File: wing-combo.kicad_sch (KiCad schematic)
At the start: 0 parts

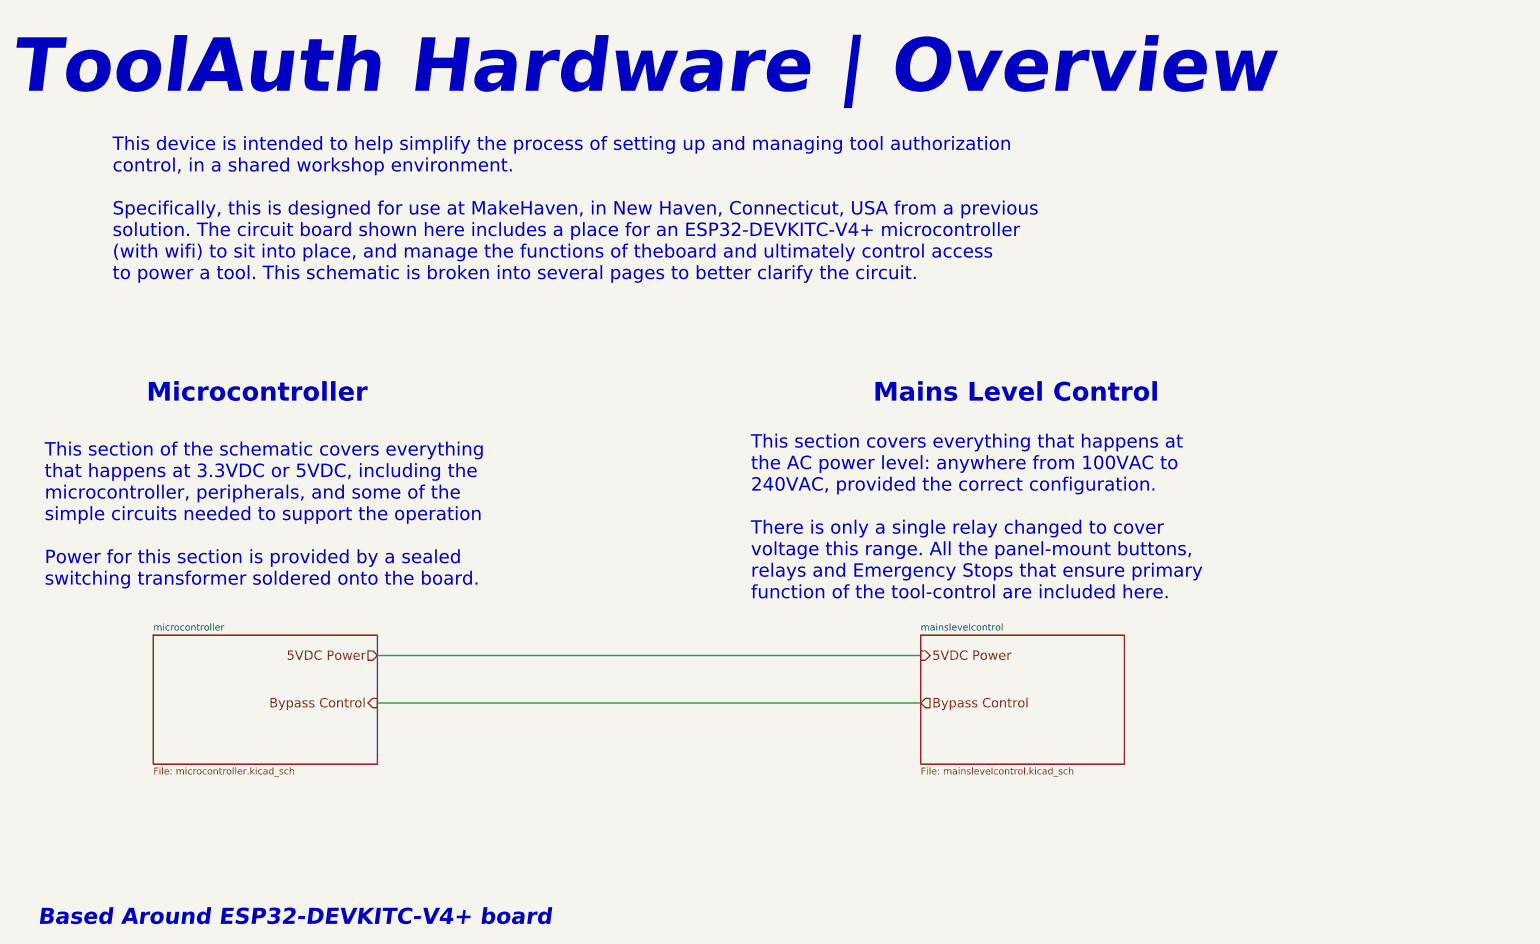
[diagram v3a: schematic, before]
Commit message: moved LED GPIO to fit free pins for ethernet wing
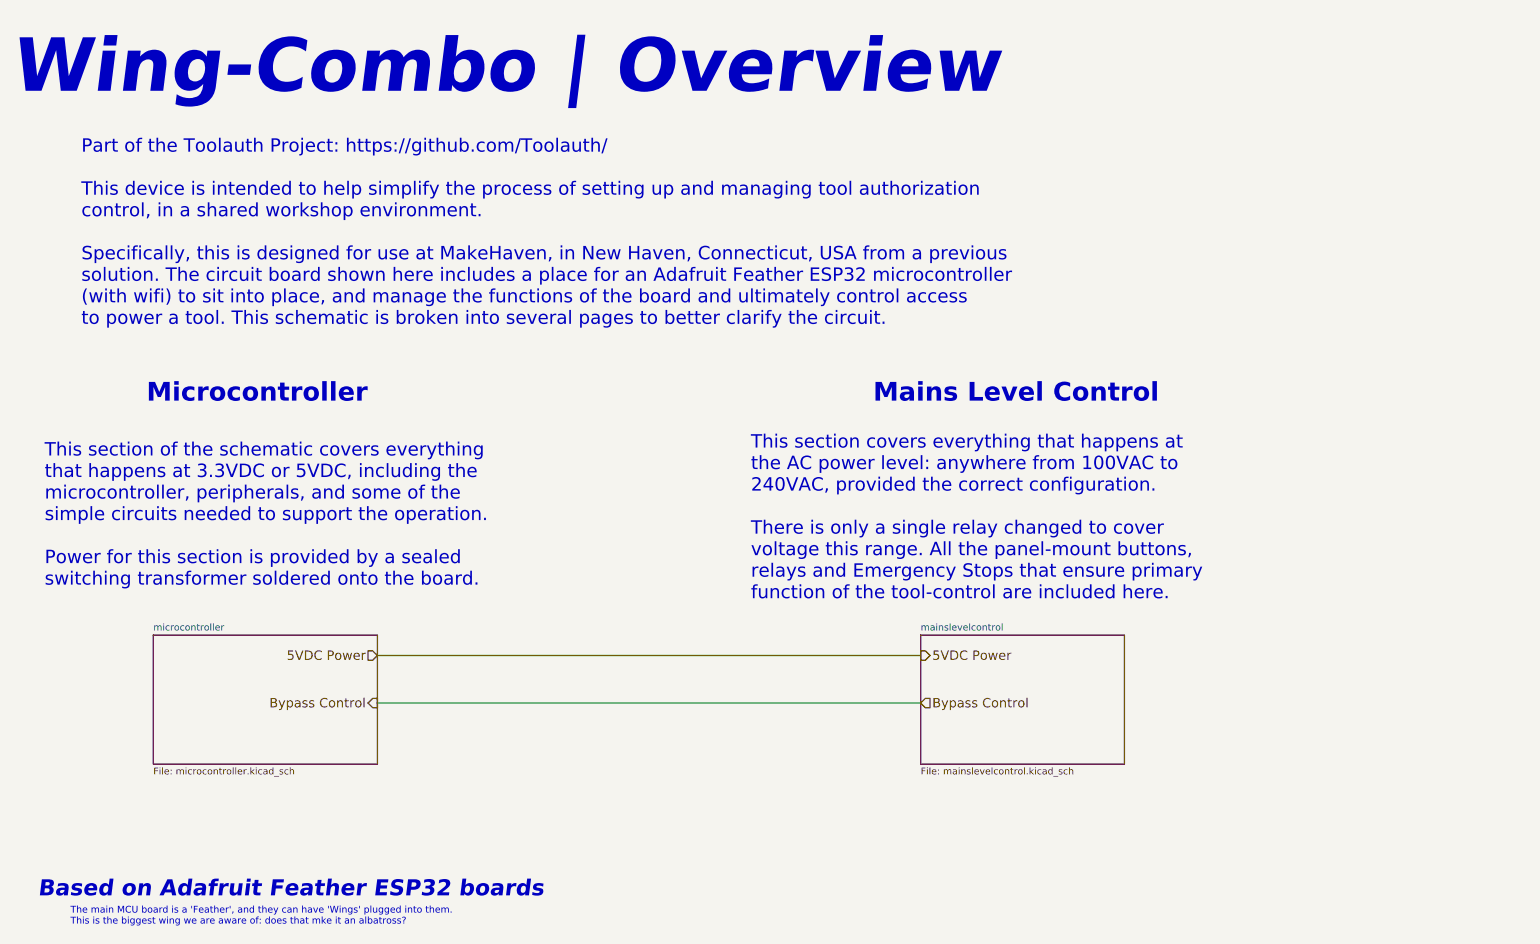
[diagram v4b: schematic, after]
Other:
- note added: "Based on Adafruit Feather ESP32 boards"
- note added: "Part of the Toolauth Project: https://github.com/Toolauth/ This device is intended to help simplify the process of setting up and managing tool authorization control, in a shared workshop environment. Specifically, this is designed for use at MakeHaven, in New Haven, Connecticut, USA from a previous solution. The circuit board shown here includes a place for an Adafruit Feather ESP32 microcontrol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"
- note added: "The main MCU board is a 'Feather', and they can have 'Wings' plugged into them. This is the biggest wing we are aware of: does that mke it an albatross?"
- note added: "This section of the schematic covers everything that happens at 3.3VDC or 5VDC, including the microcontroller, peripherals, and some of the simple circuits needed to support the operation. Power for this section is provided by a sealed switching transformer soldered onto the board."
- note added: "Wing-Combo | Overview"
- note removed: "Based Around ESP32-DEVKITC-V4+ board"
- note removed: "This device is intended to help simplify the process of setting up and managing tool authorization control, in a shared workshop environment. Specifically, this is designed for use at MakeHaven, in New Haven, Connecticut, USA from a previous solution. The circuit board shown here includes a place for an ESP32-DEVKITC-V4+ microcontroller (with wifi) to sit into place, and manage the functions of t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"
- note removed: "This section of the schematic covers everything that happens at 3.3VDC or 5VDC, including the microcontroller, peripherals, and some of the simple circuits needed to support the operation Power for this section is provided by a sealed switching transformer soldered onto the board."
- note removed: "ToolAuth Hardware | Overview"
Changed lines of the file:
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@@
 		)
 	)
-	(text "ToolAuth Hardware | Overview"
+	(text "The main MCU board is a 'Feather', and they can have 'Wings' plugged into them. \nThis is the biggest wing we are aware of: does that mke it an albatross?"
+		(exclude_from_sim no)
+		(at 34.036 189.738 0)
+		(effects
+			(font
+				(size 1.27 1.27)
+			)
+			(justify left)
+		)
+	)
+	(text "Wing-Combo | Overview"
 		(exclude_from_sim no)
 		(at 22.86 36.83 0)
@@
 		)
 	)
-	(text "This section of the schematic covers everything \nthat happens at 3.3VDC or 5VDC, including the \nmicrocontroller, peripherals, and some of the \nsimple circuits needed to support the operation \n\nPower for this section is provided by a sealed \nswitching transformer soldered onto the board. "
+	(text "This section of the schematic covers everything \nthat happens at 3.3VDC or 5VDC, including the \nmicrocontroller, peripherals, and some of the \nsimple circuits needed to support the operation.\n\nPower for this section is provided by a sealed \nswitching transformer soldered onto the board. "
 		(exclude_from_sim no)
 		(at 29.21 128.27 0)
@@
 		)
 	)
-	(text "This device is intended to help simplify the process of setting up and managing tool authorization \ncontrol, in a shared workshop environment. \n\nSpecifically, this is designed for use at MakeHaven, in New Haven, Connecticut, USA from a previous\nsolution. The circuit board shown here includes a place for an ESP32-DEVKITC-V4+ microcontroller \n(with wifi) to sit into place, and manage the functions of theboard and ultimately control access \nto power a tool. This schematic is broken into several pages to better clarify the circuit.\n"
+	(text "Part of the Toolauth Project: https://github.com/Toolauth/\n\nThis device is intended to help simplify the process of setting up and managing tool authorization \ncontrol, in a shared workshop environment. \n\nSpecifically, this is designed for use at MakeHaven, in New Haven, Connecticut, USA from a previous\nsolution. The circuit board shown here includes a place for an Adafruit Feather ESP32 microcontroller \n(with wifi) to sit into place, and manage the functions of the board and ultimately control access \nto power a tool. This schematic is broken into several pages to better clarify the circuit.\n"
 		(exclude_from_sim no)
-		(at 41.91 71.12 0)
+		(at 36.068 79.502 0)
 		(effects
 			(font
@@
 			)
 			(justify left bottom)
+			(href "https://github.com/Toolauth/")
 		)
 	)
@@
 		)
 	)
-	(text "Based Around ESP32-DEVKITC-V4+ board"
+	(text "Based on Adafruit Feather ESP32 boards"
 		(exclude_from_sim no)
-		(at 27.94 191.77 0)
+		(at 27.94 186.436 0)
 		(effects
 			(font

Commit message: 1.4.1 schematic update
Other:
- note added: "Toolauth | Wing-Combo"
- note added: "feather specification: https://learn.adafruit.com/adafruit-feather/feather-specification"
- note removed: "Wing-Combo | Overview"
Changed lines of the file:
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@@
 	(text "The main MCU board is a 'Feather', and they can have 'Wings' plugged into them. \nThis is the biggest wing we are aware of: does that mke it an albatross?"
 		(exclude_from_sim no)
-		(at 34.036 189.738 0)
+		(at 39.624 184.404 0)
 		(effects
 			(font
@@
 		)
 	)
-	(text "Wing-Combo | Overview"
+	(text "Toolauth | Wing-Combo"
 		(exclude_from_sim no)
 		(at 22.86 36.83 0)
@@
 			)
 			(justify left bottom)
+		)
+	)
+	(text "feather specification: https://learn.adafruit.com/adafruit-feather/feather-specification"
+		(exclude_from_sim no)
+		(at 80.264 190.5 0)
+		(effects
+			(font
+				(size 1.27 1.27)
+			)
+			(href "https://learn.adafruit.com/adafruit-feather/feather-specification")
 		)
 	)
@@
 	(text "Based on Adafruit Feather ESP32 boards"
 		(exclude_from_sim no)
-		(at 27.94 186.436 0)
+		(at 33.528 181.102 0)
 		(effects
 			(font

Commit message: close enough for 3D export
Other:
- note added: "The main MCU board is a 'Feather', and they can have 'Wings' plugged into them. This is the biggest wing we are aware of: does that make it an albatross?"
- note added: "This section covers everything that happens at the AC power level: anywhere from 100VAC to 240VAC, provided the corresponding configuration. There is only a single relay changed to cover voltage this range. All the panel-mount buttons, relays and Emergency Stops that ensure primary function of the tool-control are included here."
- note removed: "The main MCU board is a 'Feather', and they can have 'Wings' plugged into them. This is the biggest wing we are aware of: does that mke it an albatross?"
- note removed: "This section covers everything that happens at the AC power level: anywhere from 100VAC to 240VAC, provided the correct configuration. There is only a single relay changed to cover voltage this range. All the panel-mount buttons, relays and Emergency Stops that ensure primary function of the tool-control are included here."
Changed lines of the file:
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@@
 		)
 	)
-	(text "The main MCU board is a 'Feather', and they can have 'Wings' plugged into them. \nThis is the biggest wing we are aware of: does that mke it an albatross?"
+	(text "The main MCU board is a 'Feather', and they can have 'Wings' plugged into them. \nThis is the biggest wing we are aware of: does that make it an albatross?"
 		(exclude_from_sim no)
-		(at 39.624 184.404 0)
+		(at 41.148 181.102 0)
 		(effects
 			(font
@@
 	(text "feather specification: https://learn.adafruit.com/adafruit-feather/feather-specification"
 		(exclude_from_sim no)
-		(at 80.264 190.5 0)
+		(at 81.788 187.198 0)
 		(effects
 			(font
@@
 		)
 	)
-	(text "This section covers everything that happens at \nthe AC power level: anywhere from 100VAC to \n240VAC, provided the correct configuration. \n\nThere is only a single relay changed to cover \nvoltage this range. All the panel-mount buttons, \nrelays and Emergency Stops that ensure primary\nfunction of the tool-control are included here."
+	(text "This section covers everything that happens at \nthe AC power level: anywhere from 100VAC to \n240VAC, provided the corresponding configuration. \n\nThere is only a single relay changed to cover \nvoltage this range. All the panel-mount buttons, \nrelays and Emergency Stops that ensure primary\nfunction of the tool-control are included here."
 		(exclude_from_sim no)
 		(at 161.29 130.81 0)
@@
 	(text "Based on Adafruit Feather ESP32 boards"
 		(exclude_from_sim no)
-		(at 33.528 181.102 0)
+		(at 35.052 177.8 0)
 		(effects
 			(font
@@
 		)
 	)
-	(hierarchical_label "Bypass Control"
+	(hierarchical_label "Stage 1 Relays"
 		(shape output)
 		(at 91.44 149.86 180)
@@
 		)
 	)
-	(hierarchical_label "Bypass Control"
+	(hierarchical_label "Stage 1 Relays"
 		(shape input)
 		(at 193.04 149.86 0)
